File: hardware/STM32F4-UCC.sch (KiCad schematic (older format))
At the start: 28 parts, among them P1 Con P1, P2 Con P2, SW1 SW_PUSH, SW2 SW_PUSH, SW3 SW_PUSH, SW4 SW_PUSH

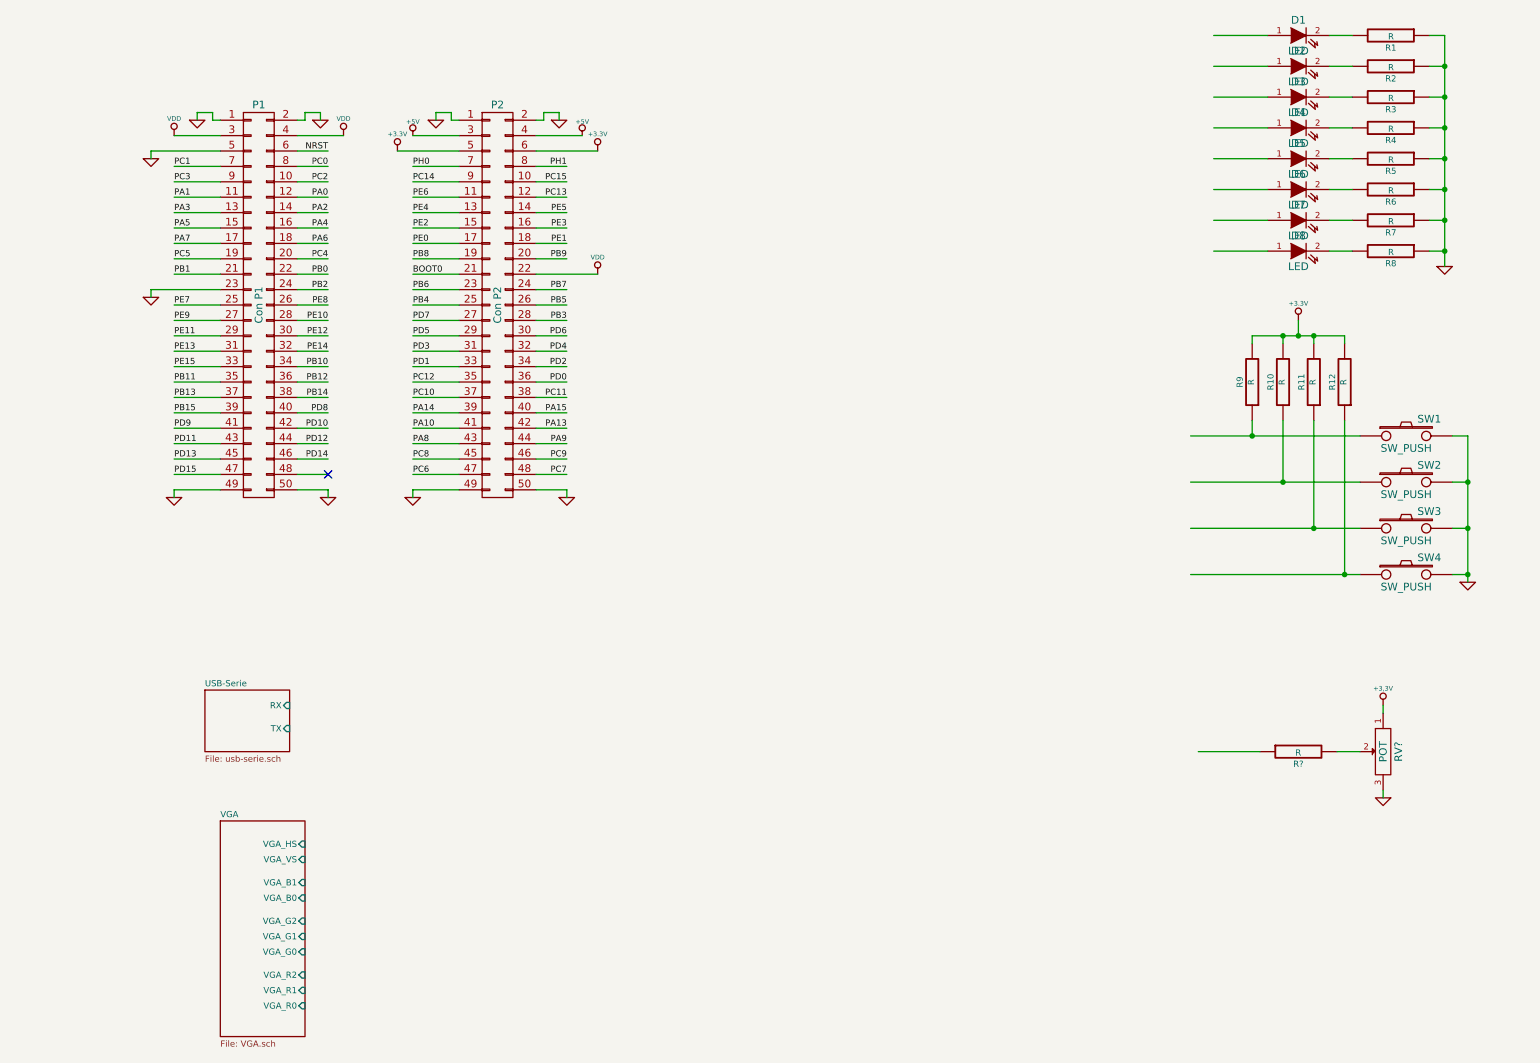
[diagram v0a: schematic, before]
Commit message: added some resistors values
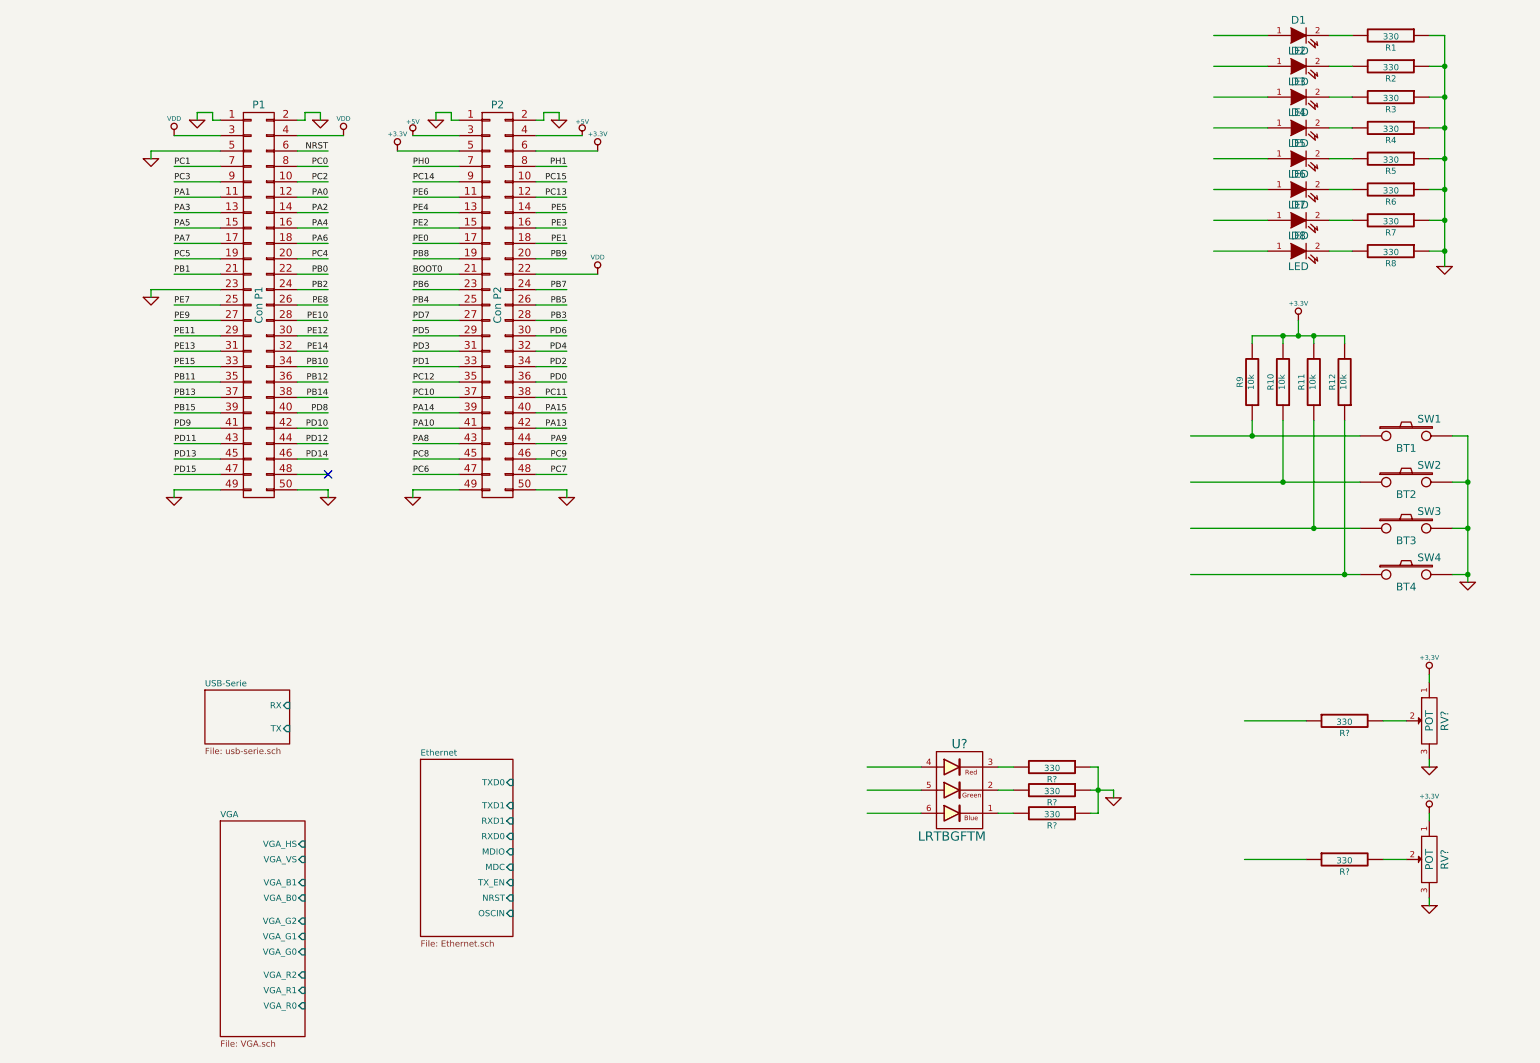
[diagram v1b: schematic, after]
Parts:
- added R? (x4): 330, symbol R
- added RV?: POT, symbol POT
- added U?: LRTBGFTM, symbol ASMT-YTC2-0AA02
- R1, R2, R3, R4, R5, R6, R7, R8, R?: value R -> 330
- R10, R11, R12, R9: value R -> 10k
- SW1: value SW_PUSH -> BT1
- SW2: value SW_PUSH -> BT2
- SW3: value SW_PUSH -> BT3
- SW4: value SW_PUSH -> BT4
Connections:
- wire segments 166 -> 181
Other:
- moved on the sheet: R?, RV?
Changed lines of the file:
@@
 LIBS:contrib
 LIBS:serial
+LIBS:oscillator-cmos-out-4
 LIBS:STM32F4-UCC-cache
 EELAYER 24 0
@@
 $Descr A4 11693 8268
 encoding utf-8
-Sheet 1 3
+Sheet 1 4
 Title "STM32 Value Line Discovery - Shiled board"
 Date "4 jun 2014"
@@
 P 10000 800
 F 0 "R1" V 10080 800 40  0000 C CNN
-F 1 "R" V 10007 801 40  0000 C CNN
+F 1 "330" V 10007 801 40  0000 C CNN
 F 2 "" V 9930 800 30  0000 C CNN
 F 3 "" H 10000 800 30  0000 C CNN
@@
 P 10000 1000
 F 0 "R2" V 10080 1000 40  0000 C CNN
-F 1 "R" V 10007 1001 40  0000 C CNN
+F 1 "330" V 10007 1001 40  0000 C CNN
 F 2 "" V 9930 1000 30  0000 C CNN
 F 3 "" H 10000 1000 30  0000 C CNN
@@
 P 10000 1200
 F 0 "R3" V 10080 1200 40  0000 C CNN
-F 1 "R" V 10007 1201 40  0000 C CNN
+F 1 "330" V 10007 1201 40  0000 C CNN
 F 2 "" V 9930 1200 30  0000 C CNN
 F 3 "" H 10000 1200 30  0000 C CNN
@@
 P 10000 1400
 F 0 "R4" V 10080 1400 40  0000 C CNN
-F 1 "R" V 10007 1401 40  0000 C CNN
+F 1 "330" V 10007 1401 40  0000 C CNN
 F 2 "" V 9930 1400 30  0000 C CNN
 F 3 "" H 10000 1400 30  0000 C CNN
@@
 P 10000 1600
 F 0 "R5" V 10080 1600 40  0000 C CNN
-F 1 "R" V 10007 1601 40  0000 C CNN
+F 1 "330" V 10007 1601 40  0000 C CNN
 F 2 "" V 9930 1600 30  0000 C CNN
 F 3 "" H 10000 1600 30  0000 C CNN
@@
 P 10000 1800
 F 0 "R6" V 10080 1800 40  0000 C CNN
-F 1 "R" V 10007 1801 40  0000 C CNN
+F 1 "330" V 10007 1801 40  0000 C CNN
 F 2 "" V 9930 1800 30  0000 C CNN
 F 3 "" H 10000 1800 30  0000 C CNN
@@
 P 10000 2000
 F 0 "R7" V 10080 2000 40  0000 C CNN
-F 1 "R" V 10007 2001 40  0000 C CNN
+F 1 "330" V 10007 2001 40  0000 C CNN
 F 2 "" V 9930 2000 30  0000 C CNN
 F 3 "" H 10000 2000 30  0000 C CNN
@@
 P 10000 2200
 F 0 "R8" V 10080 2200 40  0000 C CNN
-F 1 "R" V 10007 2201 40  0000 C CNN
+F 1 "330" V 10007 2201 40  0000 C CNN
 F 2 "" V 9930 2200 30  0000 C CNN
 F 3 "" H 10000 2200 30  0000 C CNN
@@
 P 10100 3400
 F 0 "SW1" H 10250 3510 50  0000 C CNN
-F 1 "SW_PUSH" H 10100 3320 50  0000 C CNN
+F 1 "BT1" H 10100 3320 50  0000 C CNN
 F 2 "" H 10100 3400 60  0000 C CNN
 F 3 "" H 10100 3400 60  0000 C CNN
@@
 P 10100 3700
 F 0 "SW2" H 10250 3810 50  0000 C CNN
-F 1 "SW_PUSH" H 10100 3620 50  0000 C CNN
+F 1 "BT2" H 10100 3620 50  0000 C CNN
 F 2 "" H 10100 3700 60  0000 C CNN
 F 3 "" H 10100 3700 60  0000 C CNN
@@
 P 10100 4000
 F 0 "SW3" H 10250 4110 50  0000 C CNN
-F 1 "SW_PUSH" H 10100 3920 50  0000 C CNN
+F 1 "BT3" H 10100 3920 50  0000 C CNN
 F 2 "" H 10100 4000 60  0000 C CNN
 F 3 "" H 10100 4000 60  0000 C CNN
@@
 P 10100 4300
 F 0 "SW4" H 10250 4410 50  0000 C CNN
-F 1 "SW_PUSH" H 10100 4220 50  0000 C CNN
+F 1 "BT4" H 10100 4220 50  0000 C CNN
 F 2 "" H 10100 4300 60  0000 C CNN
 F 3 "" H 10100 4300 60  0000 C CNN
@@
 P 9700 3050
 F 0 "R12" V 9780 3050 40  0000 C CNN
-F 1 "R" V 9707 3051 40  0000 C CNN
+F 1 "10k" V 9707 3051 40  0000 C CNN
 F 2 "" V 9630 3050 30  0000 C CNN
 F 3 "" H 9700 3050 30  0000 C CNN
@@
 P 9500 3050
 F 0 "R11" V 9580 3050 40  0000 C CNN
-F 1 "R" V 9507 3051 40  0000 C CNN
+F 1 "10k" V 9507 3051 40  0000 C CNN
 F 2 "" V 9430 3050 30  0000 C CNN
 F 3 "" H 9500 3050 30  0000 C CNN
@@
 P 9300 3050
 F 0 "R10" V 9380 3050 40  0000 C CNN
-F 1 "R" V 9307 3051 40  0000 C CNN
+F 1 "10k" V 9307 3051 40  0000 C CNN
 F 2 "" V 9230 3050 30  0000 C CNN
 F 3 "" H 9300 3050 30  0000 C CNN
@@
 P 9100 3050
 F 0 "R9" V 9180 3050 40  0000 C CNN
-F 1 "R" V 9107 3051 40  0000 C CNN
+F 1 "10k" V 9107 3051 40  0000 C CNN
 F 2 "" V 9030 3050 30  0000 C CNN
 F 3 "" H 9100 3050 30  0000 C CNN
@@
 Connection ~ 9400 2750
 $Sheet
-S 2300 5050 550  400
+S 2300 5050 550  350
 U 538FC087
 F0 "USB-Serie" 40
@@
 L POT RV?
 U 1 1 538FDDAB
-P 9950 5450
-F 0 "RV?" H 9950 5350 50  0000 C CNN
-F 1 "POT" H 9950 5450 50  0000 C CNN
-F 2 "" H 9950 5450 60  0000 C CNN
-F 3 "" H 9950 5450 60  0000 C CNN
-	1    9950 5450
+P 10250 5250
+F 0 "RV?" H 10250 5150 50  0000 C CNN
+F 1 "POT" H 10250 5250 50  0000 C CNN
+F 2 "" H 10250 5250 60  0000 C CNN
+F 3 "" H 10250 5250 60  0000 C CNN
+	1    10250 5250
 	0    -1   1    0
 $EndComp
@@
 L GND #PWR?
 U 1 1 538FE083
-P 9950 5750
-F 0 "#PWR?" H 9950 5750 30  0001 C CNN
-F 1 "GND" H 9950 5680 30  0001 C CNN
-F 2 "" H 9950 5750 60  0000 C CNN
-F 3 "" H 9950 5750 60  0000 C CNN
-	1    9950 5750
+P 10250 5550
+F 0 "#PWR?" H 10250 5550 30  0001 C CNN
+F 1 "GND" H 10250 5480 30  0001 C CNN
+F 2 "" H 10250 5550 60  0000 C CNN
+F 3 "" H 10250 5550 60  0000 C CNN
+	1    10250 5550
 	-1   0    0    -1
 $EndComp
 Wire Wire Line
-	9950 5750 9950 5700
+	10250 5550 10250 5500
 $Comp
 L R R?
 U 1 1 538FE166
-P 9400 5450
-F 0 "R?" V 9480 5450 40  0000 C CNN
-F 1 "R" V 9407 5451 40  0000 C CNN
-F 2 "" V 9330 5450 30  0000 C CNN
-F 3 "" H 9400 5450 30  0000 C CNN
-	1    9400 5450
+P 9700 5250
+F 0 "R?" V 9780 5250 40  0000 C CNN
+F 1 "330" V 9707 5251 40  0000 C CNN
+F 2 "" V 9630 5250 30  0000 C CNN
+F 3 "" H 9700 5250 30  0000 C CNN
+	1    9700 5250
 	0    -1   1    0
 $EndComp
 Wire Wire Line
-	9800 5450 9650 5450
+	10100 5250 9950 5250
 $Comp
 L +3,3V #PWR?
 U 1 1 538FE269
-P 9950 5150
-F 0 "#PWR?" H 9950 5110 30  0001 C CNN
-F 1 "+3,3V" H 9950 5260 30  0000 C CNN
-F 2 "" H 9950 5150 60  0000 C CNN
-F 3 "" H 9950 5150 60  0000 C CNN
-	1    9950 5150
+P 10250 4950
+F 0 "#PWR?" H 10250 4910 30  0001 C CNN
+F 1 "+3,3V" H 10250 5060 30  0000 C CNN
+F 2 "" H 10250 4950 60  0000 C CNN
+F 3 "" H 10250 4950 60  0000 C CNN
+	1    10250 4950
 	-1   0    0    -1
 $EndComp
 Wire Wire Line
-	9950 5150 9950 5200
-Wire Wire Line
-	9150 5450 8750 5450
+	10250 4950 10250 5000
+Wire Wire Line
+	9450 5250 9050 5250
 $Sheet
 S 2400 5900 550  1400
@@
 F11 "VGA_HS" I R 2950 6050 40
 $EndSheet
+$Comp
+L POT RV?
+U 1 1 53946FDE
+P 10250 6150
+F 0 "RV?" H 10250 6050 50  0000 C CNN
+F 1 "POT" H 10250 6150 50  0000 C CNN
+F 2 "" H 10250 6150 60  0000 C CNN
+F 3 "" H 10250 6150 60  0000 C CNN
+	1    10250 6150
+	0    -1   1    0
+$EndComp
+$Comp
+L GND #PWR?
+U 1 1 53946FE4
+P 10250 6450
+F 0 "#PWR?" H 10250 6450 30  0001 C CNN
+F 1 "GND" H 10250 6380 30  0001 C CNN
+F 2 "" H 10250 6450 60  0000 C CNN
+F 3 "" H 10250 6450 60  0000 C CNN
+	1    10250 6450
+	-1   0    0    -1
+$EndComp
+Wire Wire Line
+	10250 6450 10250 6400
+$Comp
+L R R?
+U 1 1 53946FEB
+P 9700 6150
+F 0 "R?" V 9780 6150 40  0000 C CNN
+F 1 "330" V 9707 6151 40  0000 C CNN
+F 2 "" V 9630 6150 30  0000 C CNN
+F 3 "" H 9700 6150 30  0000 C CNN
+	1    9700 6150
+	0    -1   1    0
+$EndComp
+Wire Wire Line
+	10100 6150 9950 6150
+$Comp
+L +3,3V #PWR?
+U 1 1 53946FF2
+P 10250 5850
+F 0 "#PWR?" H 10250 5810 30  0001 C CNN
+F 1 "+3,3V" H 10250 5960 30  0000 C CNN
+F 2 "" H 10250 5850 60  0000 C CNN
+F 3 "" H 10250 5850 60  0000 C CNN
+	1    10250 5850
+	-1   0    0    -1
+$EndComp
+Wire Wire Line
+	10250 5850 10250 5900
+Wire Wire Line
+	9450 6150 9050 6150
+$Sheet
+S 3700 5500 600  1150
+U 539471FA
+F0 "Ethernet" 40
+F1 "Ethernet.sch" 40
+F2 "TXD0" I R 4300 5650 40
+F3 "TXD1" I R 4300 5800 40
+F4 "RXD1" I R 4300 5900 40
+F5 "RXD0" I R 4300 6000 40
+F6 "MDIO" I R 4300 6100 40
+F7 "MDC" I R 4300 6200 40
+F8 "TX_EN" I R 4300 6300 40
+F9 "NRST" I R 4300 6400 40
+F10 "OSCIN" I R 4300 6500 40
+$EndSheet
+$Comp
+L ASMT-YTC2-0AA02 U?
+U 1 1 539492BE
+P 7200 5700
+F 0 "U?" H 7200 6000 60  0000 C CNN
+F 1 "LRTBGFTM" H 7150 5400 60  0000 C CNN
+F 2 "" H 7200 5700 60  0000 C CNN
+F 3 "" H 7200 5700 60  0000 C CNN
+	1    7200 5700
+	1    0    0    -1
+$EndComp
+$Comp
+L R R?
+U 1 1 5394A064
+P 7800 5550
+F 0 "R?" V 7880 5550 40  0000 C CNN
+F 1 "330" V 7807 5551 40  0000 C CNN
+F 2 "" V 7730 5550 30  0000 C CNN
+F 3 "" H 7800 5550 30  0000 C CNN
+	1    7800 5550
+	0    1    1    0
+$EndComp
+$Comp
+L R R?
+U 1 1 5394A26A
+P 7800 5700
+F 0 "R?" V 7880 5700 40  0000 C CNN
+F 1 "330" V 7807 5701 40  0000 C CNN
+F 2 "" V 7730 5700 30  0000 C CNN
+F 3 "" H 7800 5700 30  0000 C CNN
+	1    7800 5700
+	0    1    1    0
+$EndComp
+$Comp
+L R R?
+U 1 1 5394A2A5
+P 7800 5850
+F 0 "R?" V 7880 5850 40  0000 C CNN
+F 1 "330" V 7807 5851 40  0000 C CNN
+F 2 "" V 7730 5850 30  0000 C CNN
+F 3 "" H 7800 5850 30  0000 C CNN
+	1    7800 5850
+	0    1    1    0
+$EndComp
+Wire Wire Line
+	7550 5550 7450 5550
+Wire Wire Line
+	7450 5700 7550 5700
+Wire Wire Line
+	7550 5850 7450 5850
+Wire Wire Line
+	8050 5550 8100 5550
+Wire Wire Line
+	8100 5550 8100 5850
+Wire Wire Line
+	8100 5850 8050 5850
+Wire Wire Line
+	8050 5700 8200 5700
+Connection ~ 8100 5700
+$Comp
+L GND #PWR?
+U 1 1 5394A866
+P 8200 5750
+F 0 "#PWR?" H 8200 5750 30  0001 C CNN
+F 1 "GND" H 8200 5680 30  0001 C CNN
+F 2 "" H 8200 5750 60  0000 C CNN
+F 3 "" H 8200 5750 60  0000 C CNN
+	1    8200 5750
+	1    0    0    -1
+$EndComp
+Wire Wire Line
+	8200 5700 8200 5750
+Wire Wire Line
+	6950 5550 6600 5550
+Wire Wire Line
+	6950 5700 6600 5700
+Wire Wire Line
+	6950 5850 6600 5850
 $EndSCHEMATC

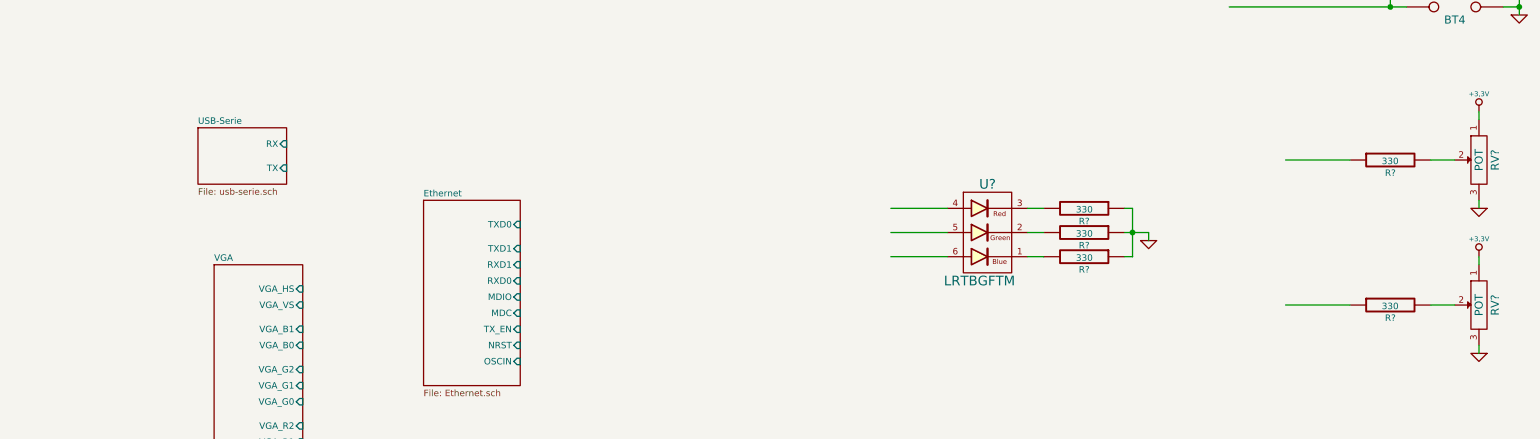
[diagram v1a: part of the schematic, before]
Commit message: Se agrego alimentacion por USB-Serie, falta fuente
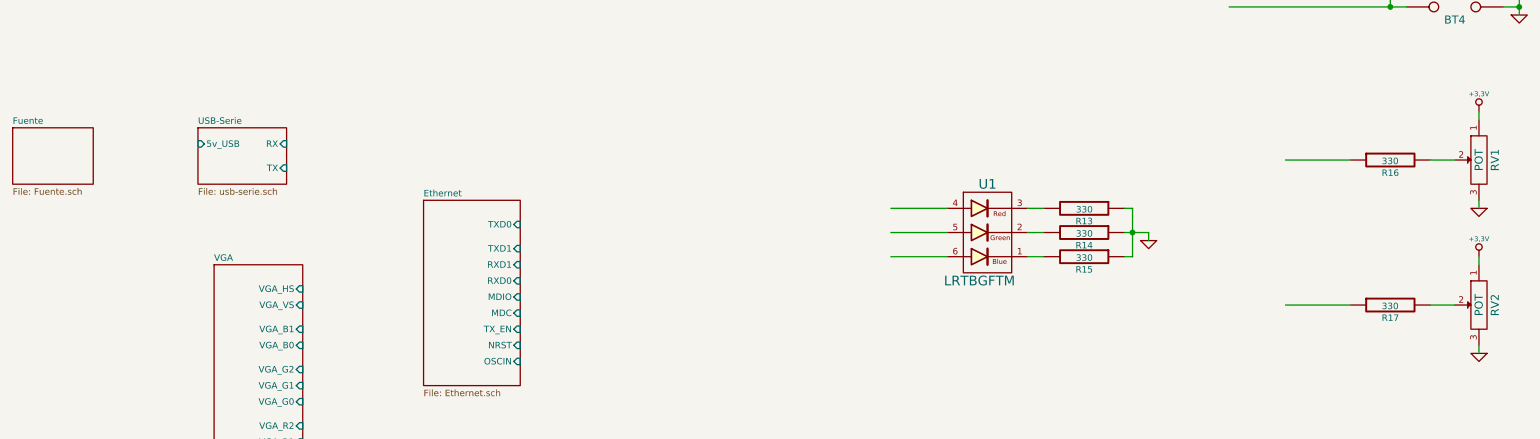
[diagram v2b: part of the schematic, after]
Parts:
- gave numbers to parts that had none: 8
